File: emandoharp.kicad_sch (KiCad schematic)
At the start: 46 parts, among them P1 piezo, P10 piezo, P2 piezo, P3 piezo, P4 piezo, P5 piezo, P6 piezo, P7 piezo, P8 piezo, P9 piezo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

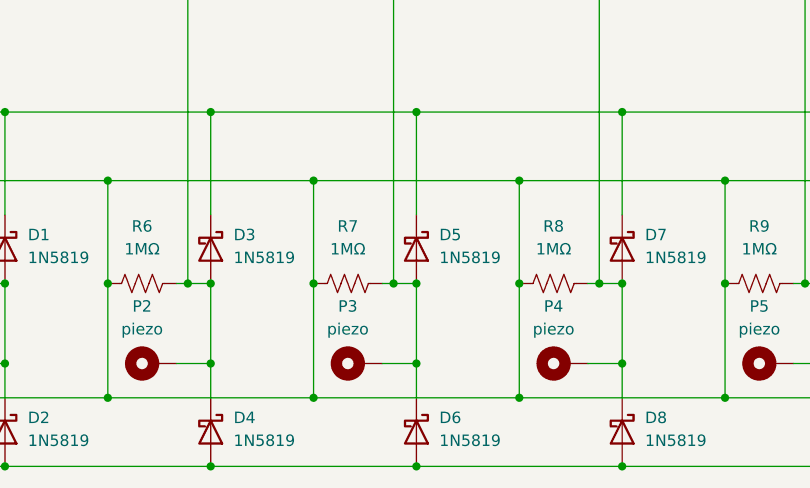
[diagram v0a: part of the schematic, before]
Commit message: remove errant junction
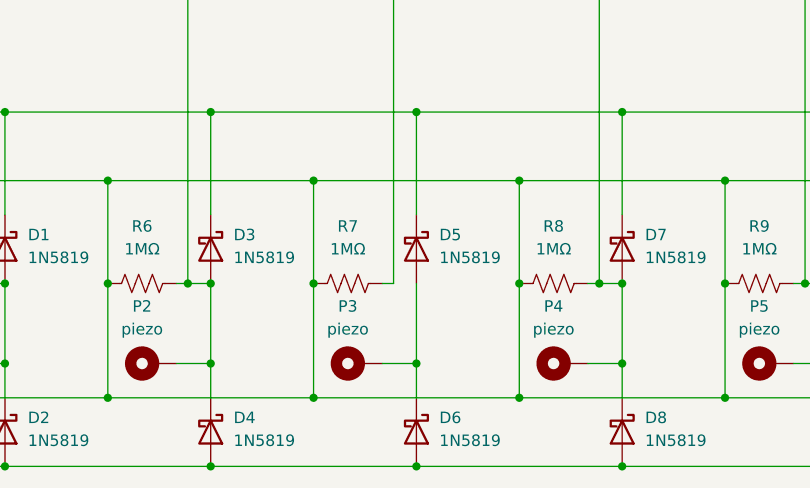
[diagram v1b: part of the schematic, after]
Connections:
- net at D5.2 (A), D6.1 (K), P3.1: no longer R7.1, U1.23 (16_A2_RX4_SCL1)
- new net: R7.1, U1.23 (16_A2_RX4_SCL1)
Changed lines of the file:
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@@
-	)
-	(junction
-		(at 102.87 170.18)
-		(diameter 0)
-		(color 0 0 0 0)
 	)
 	(junction
@@
 	)
 	(junction
-		(at 105.41 170.18)
-		(diameter 0)
-		(color 0 0 0 0)
-	)
-	(junction
 		(at 196.85 170.18)
 		(diameter 0)
@@
 		)
 		(stroke
-			(width 0)
-			(type default)
-		)
-	)
-	(wire
-		(pts
-			(xy 102.87 170.18) (xy 105.41 170.18)
-		)
-		(stroke
